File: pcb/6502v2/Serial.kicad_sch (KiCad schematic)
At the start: 10 parts, among them J10 DB9_Female, U7 MAX232, U8 W65C51NxP, Y1 1.8432 Mh

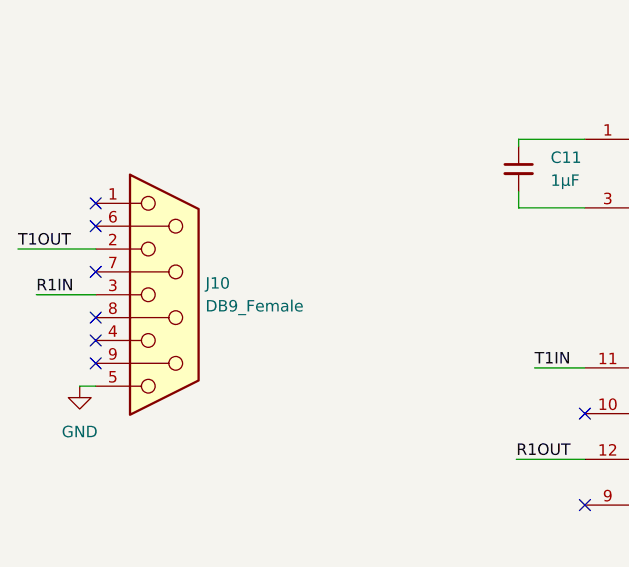
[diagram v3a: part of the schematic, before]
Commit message: First pass at routing done, now comes double checking everything
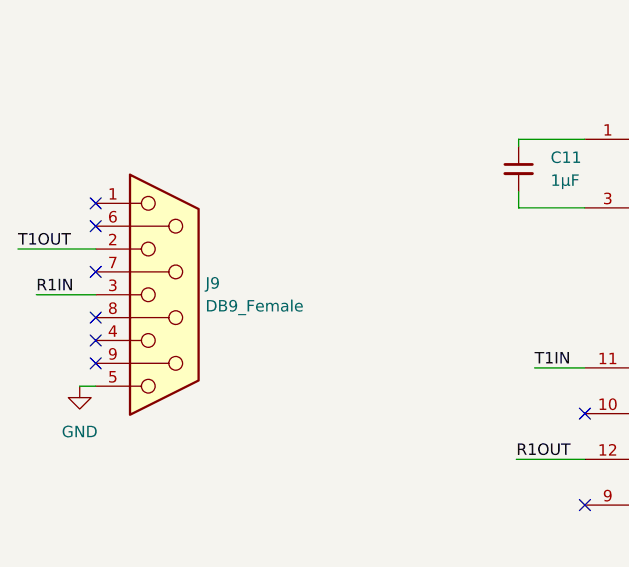
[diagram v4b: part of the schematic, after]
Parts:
- renumbered J10 to J9
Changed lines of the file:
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@@
   (symbol (lib_id "power:GND") (at 107.95 113.284 0) (unit 1)
     (in_bom yes) (on_board yes) (fields_autoplaced)
-    (property "Reference" "#PWR046" (id 0) (at 107.95 119.634 0)
+    (property "Reference" "#PWR049" (id 0) (at 107.95 119.634 0)
       (effects (font (size 1.27 1.27)) hide)
     )
@@
   (symbol (lib_id "power:GND") (at 31.496 87.376 0) (unit 1)
     (in_bom yes) (on_board yes) (fields_autoplaced)
-    (property "Reference" "#PWR044" (id 0) (at 31.496 93.726 0)
+    (property "Reference" "#PWR047" (id 0) (at 31.496 93.726 0)
       (effects (font (size 1.27 1.27)) hide)
     )
@@
   (symbol (lib_id "power:GND") (at 248.666 42.926 0) (unit 1)
     (in_bom yes) (on_board yes) (fields_autoplaced)
-    (property "Reference" "#PWR050" (id 0) (at 248.666 49.276 0)
+    (property "Reference" "#PWR053" (id 0) (at 248.666 49.276 0)
       (effects (font (size 1.27 1.27)) hide)
     )
@@
   (symbol (lib_id "power:GND") (at 202.946 108.966 0) (unit 1)
     (in_bom yes) (on_board yes) (fields_autoplaced)
-    (property "Reference" "#PWR049" (id 0) (at 202.946 115.316 0)
+    (property "Reference" "#PWR052" (id 0) (at 202.946 115.316 0)
       (effects (font (size 1.27 1.27)) hide)
     )
@@
   (symbol (lib_id "power:+5V") (at 202.946 32.258 0) (unit 1)
     (in_bom yes) (on_board yes) (fields_autoplaced)
-    (property "Reference" "#PWR048" (id 0) (at 202.946 36.068 0)
+    (property "Reference" "#PWR051" (id 0) (at 202.946 36.068 0)
       (effects (font (size 1.27 1.27)) hide)
     )
@@
   (symbol (lib_id "power:GND") (at 141.224 85.344 0) (unit 1)
     (in_bom yes) (on_board yes) (fields_autoplaced)
-    (property "Reference" "#PWR047" (id 0) (at 141.224 91.694 0)
+    (property "Reference" "#PWR050" (id 0) (at 141.224 91.694 0)
       (effects (font (size 1.27 1.27)) hide)
     )
@@
   (symbol (lib_id "power:+5V") (at 107.95 51.054 0) (unit 1)
     (in_bom yes) (on_board yes) (fields_autoplaced)
-    (property "Reference" "#PWR045" (id 0) (at 107.95 54.864 0)
+    (property "Reference" "#PWR048" (id 0) (at 107.95 54.864 0)
       (effects (font (size 1.27 1.27)) hide)
     )
@@
   (symbol (lib_id "Connector:DB9_Female") (at 40.894 77.216 0) (unit 1)
     (in_bom yes) (on_board yes) (fields_autoplaced)
-    (property "Reference" "J10" (id 0) (at 45.466 75.9459 0)
-      (effects (font (size 1.27 1.27)) (justify left))
-    )
+    (property "Reference" "J9" (id 0) (at 45.466 75.9459 0)
+      (effects (font (size 1.27 1.27)) (justify left))
+    )
